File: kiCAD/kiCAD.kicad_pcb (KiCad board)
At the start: 2 copper layers, 70 x 50 mm, 19 parts, among them J1 Analog, J2 Digital, Q1 (2N2222) 2N2222

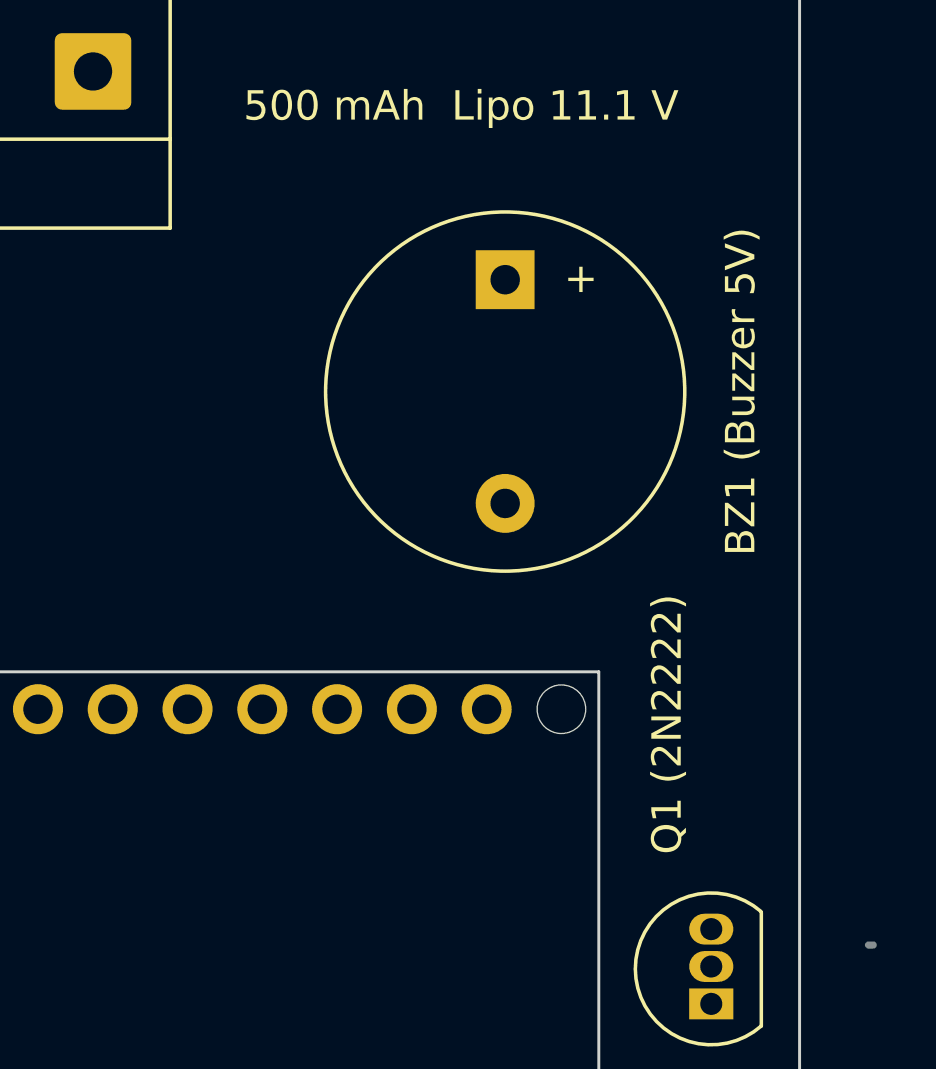
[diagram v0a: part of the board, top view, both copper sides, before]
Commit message: Minor update
Updated transitor name with BC547
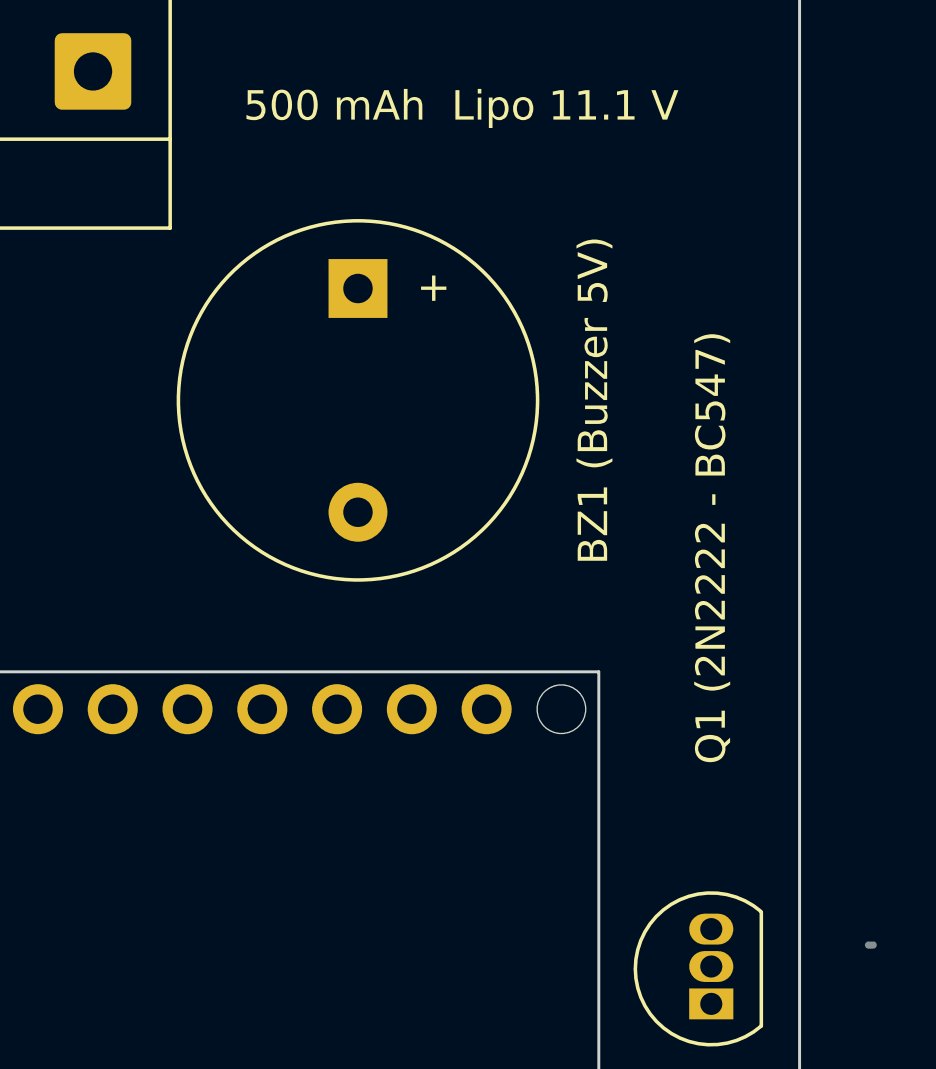
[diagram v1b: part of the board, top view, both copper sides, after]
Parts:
- Q1 (2N2222 - BC547): renamed from Q1 (2N2222)
- moved BZ1 (Buzzer 5V) 5.01 mm to (135.0, 69.2)
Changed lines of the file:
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@@
 		(descr "TO-92L leads in-line (large body variant of TO-92), also known as TO-226, wide, drill 0.75mm (see https://www.diodes.com/assets/Package-Files/TO92L.pdf and http://www.ti.com/lit/an/snoa059/snoa059.pdf)")
 		(tags "TO-92L Inline Wide transistor")
-		(property "Reference" "Q1 (2N2222)"
-			(at 9.5 -1.5 90)
+		(property "Reference" "Q1 (2N2222 - BC547)"
+			(at 15.5 0 90)
 			(layer "F.SilkS")
 			(effects
@@
 	(footprint "Buzzer_Beeper:Buzzer_12x9.5RM7.6"
 		(layer "F.Cu")
-		(at 140 68.9 -90)
+		(at 135 69.2 -90)
 		(descr "Generic Buzzer, D12mm height 9.5mm with RM7.6mm")
 		(tags "buzzer")

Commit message: Updated models
Updated models to figure out last improvements.
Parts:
- added Hole: 3.6mm, Arduino_MountingHole:MountingHole_3.2mm, F.Cu at (96.0, 91.8)
- added Hole: 3.6mm, Arduino_MountingHole:MountingHole_3.2mm, F.Cu at (169.7, 91.8)
- moved R2 (33 kOhm) 60.7 mm to (151.5, 67.4), turned to -90 degrees
- moved C1 (100nF 35V) 58.4 mm to (151.5, 85.0)
- moved BZ1 (Buzzer 5V) 53.2 mm to (165.5, 112.8), turned to 90 degrees
- moved 500 mAh  Lipo 11.1 V 44.5 mm to (168.5, 75.0), turned to 140 degrees
- moved R1 (22 kOhm) 43.0 mm to (144.0, 80.5)
- moved MPU-6050 40.8 mm to (130.0, 110.0)
- moved R3 - 6.8 kOhm 38.0 mm to (155.5, 92.5)
- moved Hole 30.1 mm to (175.5, 115.0)
- moved Hole 29.8 mm to (175.5, 68.5)
- moved Nidec_24H404H160 23.4 mm to (103.8, 71.0), turned to 90 degrees
- moved Hole 15.9 mm to (92.5, 115.0)
- moved Hole 15.5 mm to (92.5, 68.5)
- moved Q1 (2N2222 - BC547) 12.0 mm to (154.2, 103.0), turned to 180 degrees
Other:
- board size 70 x 50 mm -> 88 x 51.5 mm
